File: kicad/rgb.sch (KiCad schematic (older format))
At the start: 28 parts, among them J1 1935776, J2 Conn_01x05, J3 Conn_01x05, J4 Conn_01x04, J5 Conn_01x02, Q1 DMG9926USD, Q2 DMG9926USD, Q3 DMG9926USD, Q4 DMG9926USD, SW1 SW_Push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

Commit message: footprints
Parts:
- C1, C3, C4: footprint (none) -> Capacitor_SMD:C_0805_2012Metric_Pad1.18x1.45mm_HandSolder
- C2, C5: footprint (none) -> Capacitor_SMD:C_0603_1608Metric_Pad1.08x0.95mm_HandSolder
- D1: footprint (none) -> LED_SMD:LED_0805_2012Metric_Pad1.15x1.40mm_HandSolder
- J1: footprint (none) -> rgb_footprints:barrel jack
- J2, J3: footprint (none) -> rgb_footprints:CUI_TB003-500-P05BE
- J4: footprint (none) -> Connector_PinHeader_2.54mm:PinHeader_1x03_P2.54mm_Vertical
- J5: footprint (none) -> Connector_PinHeader_2.54mm:PinHeader_1x04_P2.54mm_Vertical
- L1: footprint (none) -> Inductor_SMD:L_1008_2520Metric_Pad1.43x2.20mm_HandSolder
- R1, R2: footprint (none) -> Resistor_SMD:R_0603_1608Metric_Pad0.98x0.95mm_HandSolder
- R3: renamed from R2; footprint (none) -> Resistor_SMD:R_0603_1608Metric_Pad0.98x0.95mm_HandSolder
- SW1, SW6: footprint (none) -> Button_Switch_THT:SW_PUSH_6mm_H13mm
- SW2, SW3, SW4, SW5: footprint (none) -> rgb_footprints:rotary encoder
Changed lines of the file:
@@
 F 0 "C3" H 5075 3075 50  0000 C CNN
 F 1 "22 uF" H 5025 3000 50  0000 L CNN
-F 2 "" H 4925 3025 50  0001 C CNN
+F 2 "Capacitor_SMD:C_0805_2012Metric_Pad1.18x1.45mm_HandSolder" H 4925 3025 50  0001 C CNN
 F 3 "~" H 4925 3025 50  0001 C CNN
 	1    4925 3025
@@
 F 0 "C4" H 5425 3075 50  0000 L CNN
 F 1 "22 uF" H 5425 3000 50  0000 L CNN
-F 2 "" H 5325 3025 50  0001 C CNN
+F 2 "Capacitor_SMD:C_0805_2012Metric_Pad1.18x1.45mm_HandSolder" H 5325 3025 50  0001 C CNN
 F 3 "~" H 5325 3025 50  0001 C CNN
 	1    5325 3025
@@
 F 0 "D1" V 5825 2975 50  0000 R CNN
 F 1 "LED" V 5750 2975 50  0000 R CNN
-F 2 "" H 5775 3050 50  0001 C CNN
+F 2 "LED_SMD:LED_0805_2012Metric_Pad1.15x1.40mm_HandSolder" H 5775 3050 50  0001 C CNN
 F 3 "~" H 5775 3050 50  0001 C CNN
 	1    5775 3050
@@
 F 0 "J4" H 4425 1100 50  0000 C CNN
 F 1 "Conn_01x04" H 4343 966 50  0001 C CNN
-F 2 "" H 4425 1300 50  0001 C CNN
+F 2 "Connector_PinHeader_2.54mm:PinHeader_1x03_P2.54mm_Vertical" H 4425 1300 50  0001 C CNN
 F 3 "~" H 4425 1300 50  0001 C CNN
 	1    4425 1300
@@
 F 0 "J5" H 5050 1100 50  0000 L CNN
 F 1 "Conn_01x02" H 5180 1301 50  0001 L CNN
-F 2 "" H 5100 1400 50  0001 C CNN
+F 2 "Connector_PinHeader_2.54mm:PinHeader_1x04_P2.54mm_Vertical" H 5100 1400 50  0001 C CNN
 F 3 "~" H 5100 1400 50  0001 C CNN
 	1    5100 1400
@@
 Text Notes 2900 1775 0    39   Italic 0
 Channel 2\n
-Text Notes 675  1275 0    39   Italic 0
+Text Notes 650  1250 0    39   Italic 0
 Power
 Wire Notes Line
@@
 F 0 "J3" H 3075 1750 50  0000 L CNN
 F 1 "Conn_01x05" H 3043 1116 50  0001 C CNN
-F 2 "" H 3125 1450 50  0001 C CNN
+F 2 "rgb_footprints:CUI_TB003-500-P05BE" H 3125 1450 50  0001 C CNN
 F 3 "~" H 3125 1450 50  0001 C CNN
 	1    3125 1450
@@
 L Connector_Generic:Conn_01x02 J1
 U 1 1 6058024D
-P 750 1150
-F 0 "J1" H 750 950 50  0000 C CNN
-F 1 "1935776" H 668 916 50  0001 C CNN
-F 2 "" H 750 1150 50  0001 C CNN
-F 3 "https://www.phoenixcontact.com/pxc-oc-itemdetail-pdf-web/eshop?lineItemType=LineItem&UID=1935776" H 750 1150 50  0001 C CNN
-	1    750  1150
-	-1   0    0    1
+P 750 1050
+F 0 "J1" H 750 1150 50  0000 C CNN
+F 1 "1935776" H 668 816 50  0001 C CNN
+F 2 "rgb_footprints:barrel jack" H 750 1050 50  0001 C CNN
+F 3 "https://www.phoenixcontact.com/pxc-oc-itemdetail-pdf-web/eshop?lineItemType=LineItem&UID=1935776" H 750 1050 50  0001 C CNN
+	1    750  1050
+	-1   0    0    -1
 $EndComp
 $Comp
@@
 F 0 "SW6" H 4175 7093 50  0000 C CNN
 F 1 "SW_Push" H 4175 7094 50  0001 C CNN
-F 2 "" H 4175 7100 50  0001 C CNN
+F 2 "Button_Switch_THT:SW_PUSH_6mm_H13mm" H 4175 7100 50  0001 C CNN
 F 3 "~" H 4175 7100 50  0001 C CNN
 	1    4175 6900
@@
 F 0 "SW5" H 4330 6075 50  0000 L CNN
 F 1 "Rotary_Encoder" H 4330 6030 50  0001 L CNN
-F 2 "" H 3950 6235 50  0001 C CNN
+F 2 "rgb_footprints:rotary encoder" H 3950 6235 50  0001 C CNN
 F 3 "~" H 4100 6335 50  0001 C CNN
 	1    4100 6075
@@
 F 0 "SW4" H 4330 5575 50  0000 L CNN
 F 1 "Rotary_Encoder" H 4330 5530 50  0001 L CNN
-F 2 "" H 3950 5735 50  0001 C CNN
+F 2 "rgb_footprints:rotary encoder" H 3950 5735 50  0001 C CNN
 F 3 "~" H 4100 5835 50  0001 C CNN
 	1    4100 5575
@@
 F 0 "SW2" H 4330 4525 50  0000 L CNN
 F 1 "Rotary_Encoder" H 4330 4480 50  0001 L CNN
-F 2 "" H 3950 4685 50  0001 C CNN
+F 2 "rgb_footprints:rotary encoder" H 3950 4685 50  0001 C CNN
 F 3 "~" H 4100 4785 50  0001 C CNN
 	1    4100 4525
@@
 F 0 "SW3" H 4330 5050 50  0000 L CNN
 F 1 "Rotary_Encoder" H 4330 5005 50  0001 L CNN
-F 2 "" H 3950 5210 50  0001 C CNN
+F 2 "rgb_footprints:rotary encoder" H 3950 5210 50  0001 C CNN
 F 3 "~" H 4100 5310 50  0001 C CNN
 	1    4100 5050
@@
 F 0 "C2" H 4225 2700 50  0000 L CNN
 F 1 "100 nF" H 4225 2625 50  0000 L CNN
-F 2 "" H 4125 2625 50  0001 C CNN
+F 2 "Capacitor_SMD:C_0603_1608Metric_Pad1.08x0.95mm_HandSolder" H 4125 2625 50  0001 C CNN
 F 3 "~" H 4125 2625 50  0001 C CNN
 	1    4125 2625
@@
 F 0 "L1" V 4775 2850 50  0000 C CNN
 F 1 "4.7 uH" V 4700 2850 50  0000 C CNN
-F 2 "" H 4625 2850 50  0001 C CNN
+F 2 "Inductor_SMD:L_1008_2520Metric_Pad1.43x2.20mm_HandSolder" H 4625 2850 50  0001 C CNN
 F 3 "~" H 4625 2850 50  0001 C CNN
 	1    4625 2850
@@
 F 0 "C1" H 2325 3075 50  0000 R CNN
 F 1 "10 uF" H 2450 3150 50  0000 R CNN
-F 2 "" H 2150 3125 50  0001 C CNN
+F 2 "Capacitor_SMD:C_0805_2012Metric_Pad1.18x1.45mm_HandSolder" H 2150 3125 50  0001 C CNN
 F 3 "~" H 2150 3125 50  0001 C CNN
 	1    2150 3125
@@
 F 0 "J2" H 2025 1750 50  0000 L CNN
 F 1 "Conn_01x05" H 2155 1401 50  0001 L CNN
-F 2 "" H 2075 1450 50  0001 C CNN
+F 2 "rgb_footprints:CUI_TB003-500-P05BE" H 2075 1450 50  0001 C CNN
 F 3 "~" H 2075 1450 50  0001 C CNN
 	1    2075 1450
@@
 F 0 "C5" H 7775 1575 50  0000 L CNN
 F 1 "100 nF" H 7600 1500 50  0000 L CNN
-F 2 "" H 8000 1525 50  0001 C CNN
+F 2 "Capacitor_SMD:C_0603_1608Metric_Pad1.08x0.95mm_HandSolder" H 8000 1525 50  0001 C CNN
 F 3 "~" H 8000 1525 50  0001 C CNN
 	1    8000 1525
@@
 	5775 3425 5775 3450
 $Comp
-L Device:R_Small_US R2
+L Device:R_Small_US R3
 U 1 1 5FEEFC54
 P 5775 3325
-F 0 "R2" H 5843 3371 50  0000 L CNN
+F 0 "R3" H 5843 3371 50  0000 L CNN
 F 1 "1 kΩ" H 5850 3300 50  0000 L CNN
-F 2 "" H 5775 3325 50  0001 C CNN
+F 2 "Resistor_SMD:R_0603_1608Metric_Pad0.98x0.95mm_HandSolder" H 5775 3325 50  0001 C CNN
 F 3 "~" H 5775 3325 50  0001 C CNN
 	1    5775 3325
@@
 F 0 "SW1" H 1125 2775 50  0000 C CNN
 F 1 "SW_Push" H 1125 2794 50  0001 C CNN
-F 2 "" H 1125 2800 50  0001 C CNN
+F 2 "Button_Switch_THT:SW_PUSH_6mm_H13mm" H 1125 2800 50  0001 C CNN
 F 3 "~" H 1125 2800 50  0001 C CNN
 	1    1125 2600
@@
 F 0 "R1" V 1625 2550 50  0000 L CNN
 F 1 "15 kΩ" V 1550 2500 50  0000 L CNN
-F 2 "" H 1475 2600 50  0001 C CNN
+F 2 "Resistor_SMD:R_0603_1608Metric_Pad0.98x0.95mm_HandSolder" H 1475 2600 50  0001 C CNN
 F 3 "~" H 1475 2600 50  0001 C CNN
 	1    1475 2600
@@
 F 0 "R2" H 1750 3175 50  0000 L CNN
 F 1 "10 kΩ" H 1750 3100 50  0000 L CNN
-F 2 "" H 1700 3125 50  0001 C CNN
+F 2 "Resistor_SMD:R_0603_1608Metric_Pad0.98x0.95mm_HandSolder" H 1700 3125 50  0001 C CNN
 F 3 "~" H 1700 3125 50  0001 C CNN
 	1    1700 3125
@@
 $EndComp
 $Comp
-L power:GND #PWR?
+L power:GND #PWR0112
 U 1 1 6001B645
 P 1700 3275
-F 0 "#PWR?" H 1700 3025 50  0001 C CNN
+F 0 "#PWR0112" H 1700 3025 50  0001 C CNN
 F 1 "GND" H 1700 3125 50  0000 C CNN
 F 2 "" H 1700 3275 50  0001 C CNN

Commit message: Changed dc-dc
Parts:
- removed C2: 100 nF, Capacitor_SMD:C_0603_1608Metric_Pad1.08x0.95mm_HandSolder, symbol Device:C_Small
- removed C3, C4: 22 uF, Capacitor_SMD:C_0805_2012Metric_Pad1.18x1.45mm_HandSolder, symbol Device:C_Small
- removed L1: 4.7 uH, Inductor_SMD:L_1008_2520Metric_Pad1.43x2.20mm_HandSolder, symbol Device:L
- removed U2: AP63205WU-7, rgb_footprints:AP63205WU-7, symbol AP63205WU:AP63205WU-7
- added C1: 100 uF, symbol Device:CP1
- added U2: MIC5203, SOT-143_M4_MCH, symbol MIC5203:MIC5203-5.0YM4-TR
- C1: value 10 uF -> 470 nF; footprint Capacitor_SMD:C_0805_2012Metric_Pad1.18x1.45mm_HandSolder -> Capacitor_SMD:C_0805_2012Metric_Pad1.15x1.40mm_HandSolder
- R1: value 15 kΩ -> 100k; footprint Resistor_SMD:R_0603_1608Metric_Pad0.98x0.95mm_HandSolder -> (none)
- R2: value 10 kΩ -> 50k; footprint Resistor_SMD:R_0603_1608Metric_Pad0.98x0.95mm_HandSolder -> (none)
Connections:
- wire segments 153 -> 139
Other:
- moved on the sheet: C5, D1, J2, J3, J4, J5, Q1A, Q1B, Q2A, Q2B, Q3A, Q3B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

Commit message: bulk capacitor
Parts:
- C1: value 100 uF -> 220 uF; footprint (none) -> Capacitor_SMD:CP_Elec_6.3x7.7
- R1, R2: footprint (none) -> Resistor_SMD:R_0603_1608Metric_Pad1.05x0.95mm_HandSolder
- U2: footprint SOT-143_M4_MCH -> digikey-footprints:SOT-143-4
- renumbered C1 to C3, C5 to C4
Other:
- moved on the sheet: C1, J2, J3, J4

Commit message: layout start
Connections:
- net DRAIN_5: now also Q3.D2; no longer Q3.D1 (D2)
- net DRAIN_6: now also Q3.D1 (D2); no longer Q3.D2
- net DRAIN_7: now also Q4.D2; no longer Q4.D1 (D2)
- net DRAIN_8: now also Q4.D1 (D2); no longer Q4.D2
- net GND: now also Q3.S1 (S2), Q3.S2, Q4.S1 (S2), Q4.S2; no longer Q3.S1 (S2), Q3.S2, Q4.S1 (S2), Q4.S2
- net PWM_5: now also Q3.G2; no longer Q3.G1 (G2)
- net PWM_6: now also Q3.G1 (G2); no longer Q3.G2
- net PWM_7: now also Q4.G2; no longer Q4.G1 (G2)
- net PWM_8: now also Q4.G1 (G2); no longer Q4.G2
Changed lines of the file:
@@
 $Comp
 L mosfet:DMG9926USD Q4
-U 2 1 602258A6
+U 1 1 602258A6
 P 7425 4000
 F 0 "Q4" H 7550 4000 50  0000 L CNN
@@
 F 2 "rgb_footprints:DMG9926USD_Handsolder" H 7325 3500 50  0001 C CNN
 F 3 "https://www.diodes.com/assets/Datasheets/ds31757.pdf" H 6850 4160 50  0001 C CNN
-	2    7425 4000
+	1    7425 4000
 	1    0    0    -1
 $EndComp
 Wire Wire Line
 	6925 3100 7175 3100
-Text Label 6925 3100 0    50   ~ 0
-PWM_6
 Wire Wire Line
 	7475 3300 7475 3350
@@
 	1    0    0    -1
 $EndComp
-Text Label 7925 2850 2    50   ~ 0
-DRAIN_6
 Wire Wire Line
 	7475 2850 7925 2850
@@
 $Comp
 L mosfet:DMG9926USD Q3
-U 2 1 60225894
+U 1 1 60225894
 P 7425 3100
 F 0 "Q3" H 7550 3100 50  0000 L CNN
@@
 F 2 "rgb_footprints:DMG9926USD_Handsolder" H 7325 2600 50  0001 C CNN
 F 3 "https://www.diodes.com/assets/Datasheets/ds31757.pdf" H 6850 3260 50  0001 C CNN
-	2    7425 3100
+	1    7425 3100
 	1    0    0    -1
 $EndComp
@@
 $Comp
 L mosfet:DMG9926USD Q4
-U 1 1 5FEAD256
+U 2 1 5FEAD256
 P 6100 4000
 F 0 "Q4" H 6225 4000 50  0000 L CNN
@@
 F 2 "rgb_footprints:DMG9926USD_Handsolder" H 6000 3500 50  0001 C CNN
 F 3 "https://www.diodes.com/assets/Datasheets/ds31757.pdf" H 5525 4160 50  0001 C CNN
-	1    6100 4000
+	2    6100 4000
 	1    0    0    -1
 $EndComp
@@
 $Comp
 L mosfet:DMG9926USD Q3
-U 1 1 5FEAD244
+U 2 1 5FEAD244
 P 6100 3100
 F 0 "Q3" H 6225 3100 50  0000 L CNN
@@
 F 2 "rgb_footprints:DMG9926USD_Handsolder" H 6000 2600 50  0001 C CNN
 F 3 "https://www.diodes.com/assets/Datasheets/ds31757.pdf" H 5525 3260 50  0001 C CNN
-	1    6100 3100
+	2    6100 3100
 	1    0    0    -1
 $EndComp
@@
 Wire Wire Line
 	1375 1050 1600 1050
+Text Label 6925 3100 0    50   ~ 0
+PWM_6
+Text Label 7925 2850 2    50   ~ 0
+DRAIN_6
 $EndSCHEMATC

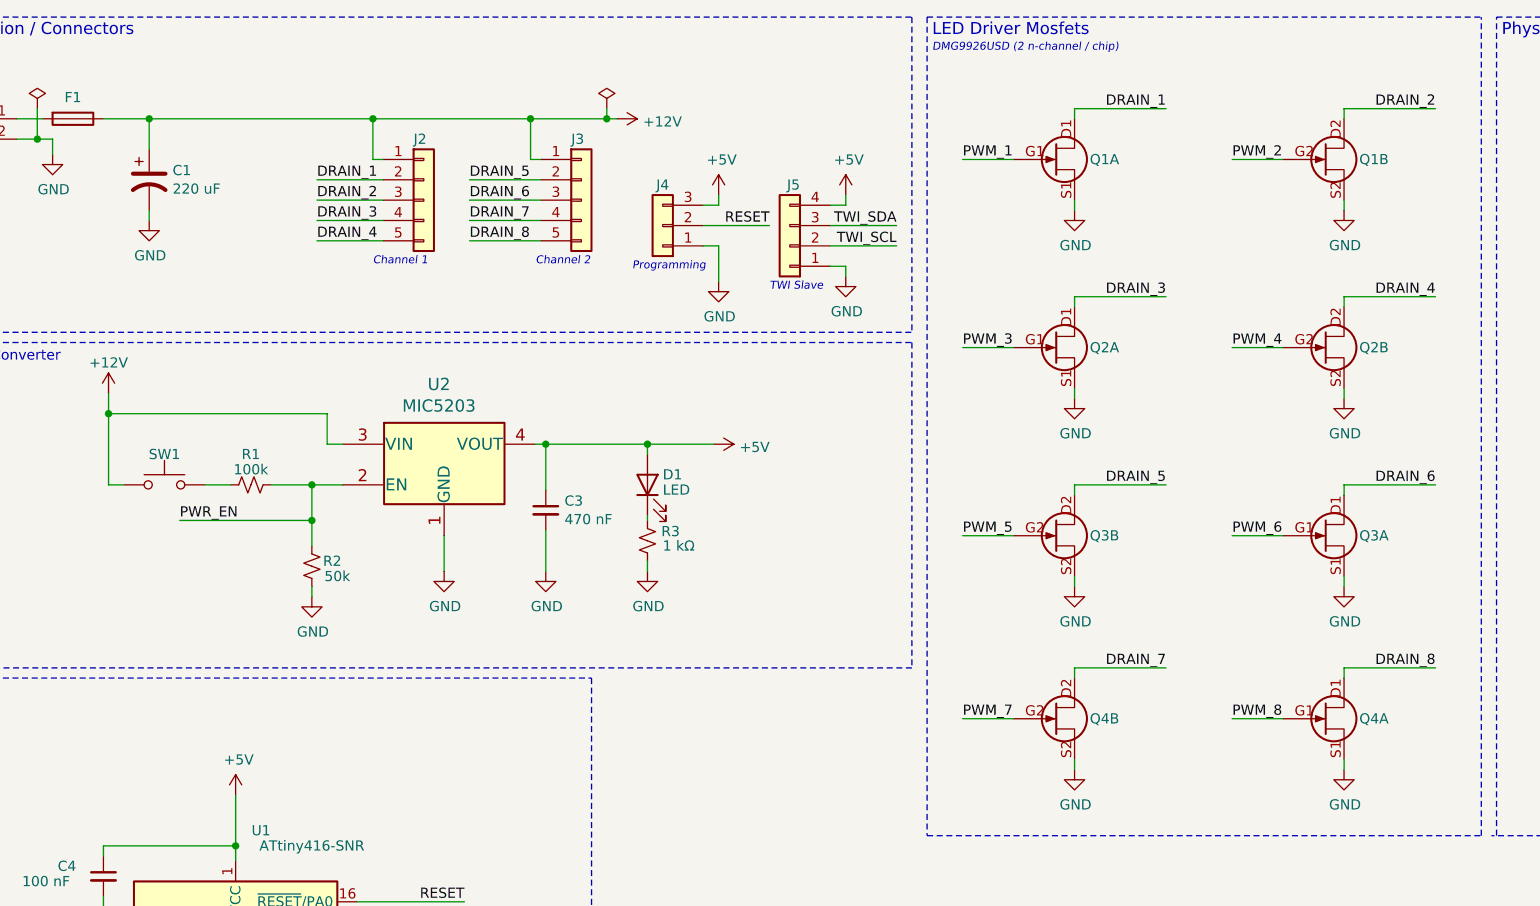
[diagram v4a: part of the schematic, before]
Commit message: ground / power planes
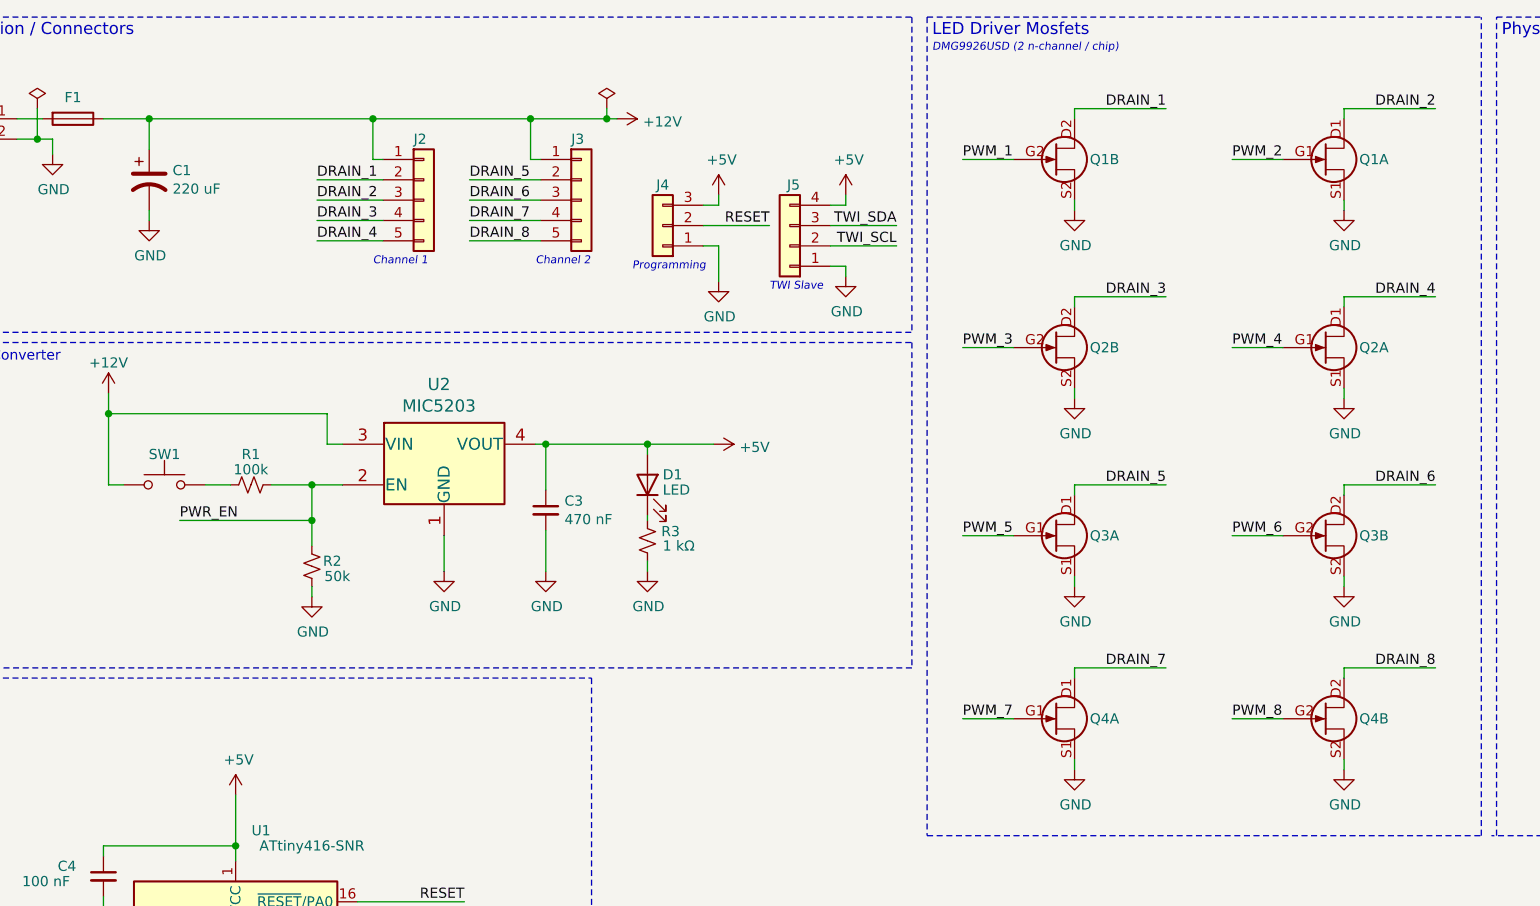
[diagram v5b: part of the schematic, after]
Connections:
- net +12V: now also SW1.2; no longer SW1.1
- net DRAIN_1: now also Q1.D2; no longer Q1.D1 (D2)
- net DRAIN_2: now also Q1.D1 (D2); no longer Q1.D2
- net DRAIN_3: now also Q2.D2; no longer Q2.D1 (D2)
- net DRAIN_4: now also Q2.D1 (D2); no longer Q2.D2
- net DRAIN_5: now also Q3.D1 (D2); no longer Q3.D2
- net DRAIN_6: now also Q3.D2; no longer Q3.D1 (D2)
- net DRAIN_7: now also Q4.D1 (D2); no longer Q4.D2
- net DRAIN_8: now also Q4.D2; no longer Q4.D1 (D2)
- net GND: now also Q1.S1 (S2), Q1.S2, Q2.S1 (S2), Q2.S2, Q3.S1 (S2), Q3.S2, Q4.S1 (S2), Q4.S2; no longer Q1.S1 (S2), Q1.S2, Q2.S1 (S2), Q2.S2, Q3.S1 (S2), Q3.S2, Q4.S1 (S2), Q4.S2
- net PWM_1: now also Q1.G2; no longer Q1.G1 (G2)
- net PWM_2: now also Q1.G1 (G2); no longer Q1.G2
- net PWM_3: now also Q2.G2; no longer Q2.G1 (G2)
- net PWM_4: now also Q2.G1 (G2); no longer Q2.G2
- net PWM_5: now also Q3.G1 (G2); no longer Q3.G2
- net PWM_6: now also Q3.G2; no longer Q3.G1 (G2)
- net PWM_7: now also Q4.G1 (G2); no longer Q4.G2
- net PWM_8: now also Q4.G2; no longer Q4.G1 (G2)
- net at R1.2: now also SW1.1; no longer SW1.2
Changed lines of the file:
@@
 $Comp
 L mosfet:DMG9926USD Q4
-U 1 1 602258A6
+U 2 1 602258A6
 P 7425 4000
 F 0 "Q4" H 7550 4000 50  0000 L CNN
@@
 F 2 "rgb_footprints:DMG9926USD_Handsolder" H 7325 3500 50  0001 C CNN
 F 3 "https://www.diodes.com/assets/Datasheets/ds31757.pdf" H 6850 4160 50  0001 C CNN
-	1    7425 4000
+	2    7425 4000
 	1    0    0    -1
 $EndComp
@@
 $Comp
 L mosfet:DMG9926USD Q3
-U 1 1 60225894
+U 2 1 60225894
 P 7425 3100
 F 0 "Q3" H 7550 3100 50  0000 L CNN
@@
 F 2 "rgb_footprints:DMG9926USD_Handsolder" H 7325 2600 50  0001 C CNN
 F 3 "https://www.diodes.com/assets/Datasheets/ds31757.pdf" H 6850 3260 50  0001 C CNN
-	1    7425 3100
+	2    7425 3100
 	1    0    0    -1
 $EndComp
@@
 $Comp
 L mosfet:DMG9926USD Q2
-U 2 1 60225882
+U 1 1 60225882
 P 7425 2175
 F 0 "Q2" H 7550 2175 50  0000 L CNN
@@
 F 2 "rgb_footprints:DMG9926USD_Handsolder" H 7325 1675 50  0001 C CNN
 F 3 "https://www.diodes.com/assets/Datasheets/ds31757.pdf" H 6850 2335 50  0001 C CNN
-	2    7425 2175
+	1    7425 2175
 	1    0    0    -1
 $EndComp
@@
 $Comp
 L mosfet:DMG9926USD Q1
-U 2 1 60225873
+U 1 1 60225873
 P 7425 1250
 F 0 "Q1" H 7550 1250 50  0000 L CNN
@@
 F 2 "rgb_footprints:DMG9926USD_Handsolder" H 7325 750 50  0001 C CNN
 F 3 "https://www.diodes.com/assets/Datasheets/ds31757.pdf" H 6850 1410 50  0001 C CNN
-	2    7425 1250
+	1    7425 1250
 	1    0    0    -1
 $EndComp
@@
 $Comp
 L mosfet:DMG9926USD Q4
-U 2 1 5FEAD256
+U 1 1 5FEAD256
 P 6100 4000
 F 0 "Q4" H 6225 4000 50  0000 L CNN
@@
 F 2 "rgb_footprints:DMG9926USD_Handsolder" H 6000 3500 50  0001 C CNN
 F 3 "https://www.diodes.com/assets/Datasheets/ds31757.pdf" H 5525 4160 50  0001 C CNN
-	2    6100 4000
+	1    6100 4000
 	1    0    0    -1
 $EndComp
@@
 $Comp
 L mosfet:DMG9926USD Q3
-U 2 1 5FEAD244
+U 1 1 5FEAD244
 P 6100 3100
 F 0 "Q3" H 6225 3100 50  0000 L CNN
@@
 F 2 "rgb_footprints:DMG9926USD_Handsolder" H 6000 2600 50  0001 C CNN
 F 3 "https://www.diodes.com/assets/Datasheets/ds31757.pdf" H 5525 3260 50  0001 C CNN
-	2    6100 3100
+	1    6100 3100
 	1    0    0    -1
 $EndComp
@@
 $Comp
 L mosfet:DMG9926USD Q2
-U 1 1 5FEA7092
+U 2 1 5FEA7092
 P 6100 2175
 F 0 "Q2" H 6225 2175 50  0000 L CNN
@@
 F 2 "rgb_footprints:DMG9926USD_Handsolder" H 6000 1675 50  0001 C CNN
 F 3 "https://www.diodes.com/assets/Datasheets/ds31757.pdf" H 5525 2335 50  0001 C CNN
-	1    6100 2175
+	2    6100 2175
 	1    0    0    -1
 $EndComp
@@
 $Comp
 L mosfet:DMG9926USD Q1
-U 1 1 5FE90B41
+U 2 1 5FE90B41
 P 6100 1250
 F 0 "Q1" H 6225 1250 50  0000 L CNN
@@
 F 2 "rgb_footprints:DMG9926USD_Handsolder" H 6000 750 50  0001 C CNN
 F 3 "https://www.diodes.com/assets/Datasheets/ds31757.pdf" H 5525 1410 50  0001 C CNN
-	1    6100 1250
+	2    6100 1250
 	1    0    0    -1
 $EndComp
@@
 F 3 "~" H 1675 3050 50  0001 C CNN
 	1    1675 2850
-	1    0    0    -1
-$EndComp
-Wire Wire Line
+	-1   0    0    -1
+$EndComp
+Wire Wire Line
